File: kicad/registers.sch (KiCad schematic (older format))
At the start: 0 parts

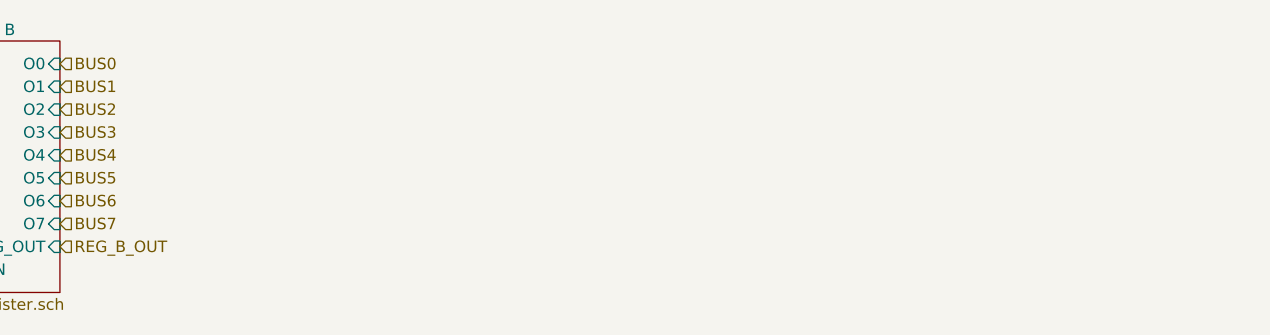
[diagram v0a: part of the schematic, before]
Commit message: Add M0-2 registers
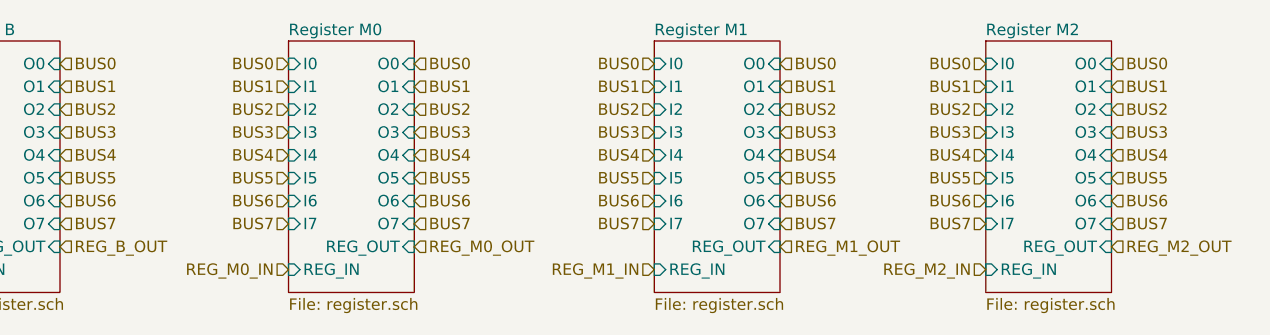
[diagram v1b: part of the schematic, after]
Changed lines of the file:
@@
 $Descr A4 11693 8268
 encoding utf-8
-Sheet 5 9
+Sheet 5 15
 Title ""
 Date ""
@@
 Text HLabel 3050 1650 2    50   Input ~ 0
 REG_B_OUT
+$Sheet
+S 4050 750  550  1100
+U 5AFCB536
+F0 "Register M0" 50
+F1 "register.sch" 50
+F2 "REG_IN" I L 4050 1750 50
+F3 "I0" I L 4050 850 50
+F4 "I1" I L 4050 950 50
+F5 "I2" I L 4050 1050 50
+F6 "I3" I L 4050 1150 50
+F7 "I4" I L 4050 1250 50
+F8 "I5" I L 4050 1350 50
+F9 "I6" I L 4050 1450 50
+F10 "I7" I L 4050 1550 50
+F11 "REG_OUT" I R 4600 1650 50
+F12 "O0" I R 4600 850 50
+F13 "O1" I R 4600 950 50
+F14 "O2" I R 4600 1050 50
+F15 "O3" I R 4600 1150 50
+F16 "O4" I R 4600 1250 50
+F17 "O5" I R 4600 1350 50
+F18 "O6" I R 4600 1450 50
+F19 "O7" I R 4600 1550 50
+$EndSheet
+Text HLabel 4050 850  0    50   Input ~ 0
+BUS0
+Text HLabel 4050 950  0    50   Input ~ 0
+BUS1
+Text HLabel 4050 1050 0    50   Input ~ 0
+BUS2
+Text HLabel 4050 1150 0    50   Input ~ 0
+BUS3
+Text HLabel 4050 1250 0    50   Input ~ 0
+BUS4
+Text HLabel 4050 1350 0    50   Input ~ 0
+BUS5
+Text HLabel 4050 1450 0    50   Input ~ 0
+BUS6
+Text HLabel 4050 1550 0    50   Input ~ 0
+BUS7
+Text HLabel 4600 850  2    50   Input ~ 0
+BUS0
+Text HLabel 4600 950  2    50   Input ~ 0
+BUS1
+Text HLabel 4600 1050 2    50   Input ~ 0
+BUS2
+Text HLabel 4600 1150 2    50   Input ~ 0
+BUS3
+Text HLabel 4600 1250 2    50   Input ~ 0
+BUS4
+Text HLabel 4600 1350 2    50   Input ~ 0
+BUS5
+Text HLabel 4600 1450 2    50   Input ~ 0
+BUS6
+Text HLabel 4600 1550 2    50   Input ~ 0
+BUS7
+Text HLabel 4050 1750 0    50   Input ~ 0
+REG_M0_IN
+Text HLabel 4600 1650 2    50   Input ~ 0
+REG_M0_OUT
+$Sheet
+S 5650 750  550  1100
+U 5AFCB55D
+F0 "Register M1" 50
+F1 "register.sch" 50
+F2 "REG_IN" I L 5650 1750 50
+F3 "I0" I L 5650 850 50
+F4 "I1" I L 5650 950 50
+F5 "I2" I L 5650 1050 50
+F6 "I3" I L 5650 1150 50
+F7 "I4" I L 5650 1250 50
+F8 "I5" I L 5650 1350 50
+F9 "I6" I L 5650 1450 50
+F10 "I7" I L 5650 1550 50
+F11 "REG_OUT" I R 6200 1650 50
+F12 "O0" I R 6200 850 50
+F13 "O1" I R 6200 950 50
+F14 "O2" I R 6200 1050 50
+F15 "O3" I R 6200 1150 50
+F16 "O4" I R 6200 1250 50
+F17 "O5" I R 6200 1350 50
+F18 "O6" I R 6200 1450 50
+F19 "O7" I R 6200 1550 50
+$EndSheet
+Text HLabel 5650 850  0    50   Input ~ 0
+BUS0
+Text HLabel 5650 950  0    50   Input ~ 0
+BUS1
+Text HLabel 5650 1050 0    50   Input ~ 0
+BUS2
+Text HLabel 5650 1150 0    50   Input ~ 0
+BUS3
+Text HLabel 5650 1250 0    50   Input ~ 0
+BUS4
+Text HLabel 5650 1350 0    50   Input ~ 0
+BUS5
+Text HLabel 5650 1450 0    50   Input ~ 0
+BUS6
+Text HLabel 5650 1550 0    50   Input ~ 0
+BUS7
+Text HLabel 6200 850  2    50   Input ~ 0
+BUS0
+Text HLabel 6200 950  2    50   Input ~ 0
+BUS1
+Text HLabel 6200 1050 2    50   Input ~ 0
+BUS2
+Text HLabel 6200 1150 2    50   Input ~ 0
+BUS3
+Text HLabel 6200 1250 2    50   Input ~ 0
+BUS4
+Text HLabel 6200 1350 2    50   Input ~ 0
+BUS5
+Text HLabel 6200 1450 2    50   Input ~ 0
+BUS6
+Text HLabel 6200 1550 2    50   Input ~ 0
+BUS7
+Text HLabel 5650 1750 0    50   Input ~ 0
+REG_M1_IN
+Text HLabel 6200 1650 2    50   Input ~ 0
+REG_M1_OUT
+$Sheet
+S 7100 750  550  1100
+U 5AFCB584
+F0 "Register M2" 50
+F1 "register.sch" 50
+F2 "REG_IN" I L 7100 1750 50
+F3 "I0" I L 7100 850 50
+F4 "I1" I L 7100 950 50
+F5 "I2" I L 7100 1050 50
+F6 "I3" I L 7100 1150 50
+F7 "I4" I L 7100 1250 50
+F8 "I5" I L 7100 1350 50
+F9 "I6" I L 7100 1450 50
+F10 "I7" I L 7100 1550 50
+F11 "REG_OUT" I R 7650 1650 50
+F12 "O0" I R 7650 850 50
+F13 "O1" I R 7650 950 50
+F14 "O2" I R 7650 1050 50
+F15 "O3" I R 7650 1150 50
+F16 "O4" I R 7650 1250 50
+F17 "O5" I R 7650 1350 50
+F18 "O6" I R 7650 1450 50
+F19 "O7" I R 7650 1550 50
+$EndSheet
+Text HLabel 7100 850  0    50   Input ~ 0
+BUS0
+Text HLabel 7100 950  0    50   Input ~ 0
+BUS1
+Text HLabel 7100 1050 0    50   Input ~ 0
+BUS2
+Text HLabel 7100 1150 0    50   Input ~ 0
+BUS3
+Text HLabel 7100 1250 0    50   Input ~ 0
+BUS4
+Text HLabel 7100 1350 0    50   Input ~ 0
+BUS5
+Text HLabel 7100 1450 0    50   Input ~ 0
+BUS6
+Text HLabel 7100 1550 0    50   Input ~ 0
+BUS7
+Text HLabel 7650 850  2    50   Input ~ 0
+BUS0
+Text HLabel 7650 950  2    50   Input ~ 0
+BUS1
+Text HLabel 7650 1050 2    50   Input ~ 0
+BUS2
+Text HLabel 7650 1150 2    50   Input ~ 0
+BUS3
+Text HLabel 7650 1250 2    50   Input ~ 0
+BUS4
+Text HLabel 7650 1350 2    50   Input ~ 0
+BUS5
+Text HLabel 7650 1450 2    50   Input ~ 0
+BUS6
+Text HLabel 7650 1550 2    50   Input ~ 0
+BUS7
+Text HLabel 7100 1750 0    50   Input ~ 0
+REG_M2_IN
+Text HLabel 7650 1650 2    50   Input ~ 0
+REG_M2_OUT
 $EndSCHEMATC

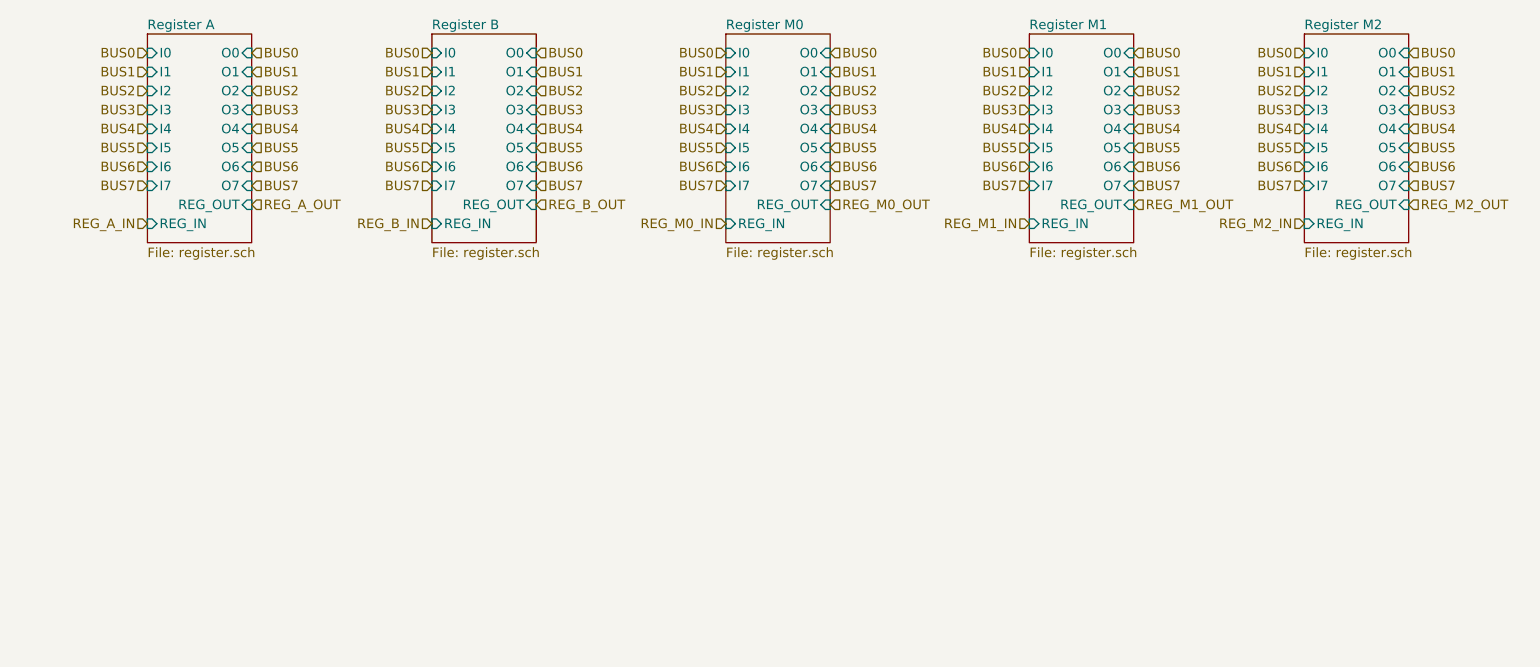
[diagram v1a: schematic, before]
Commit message: Remove register LEDs
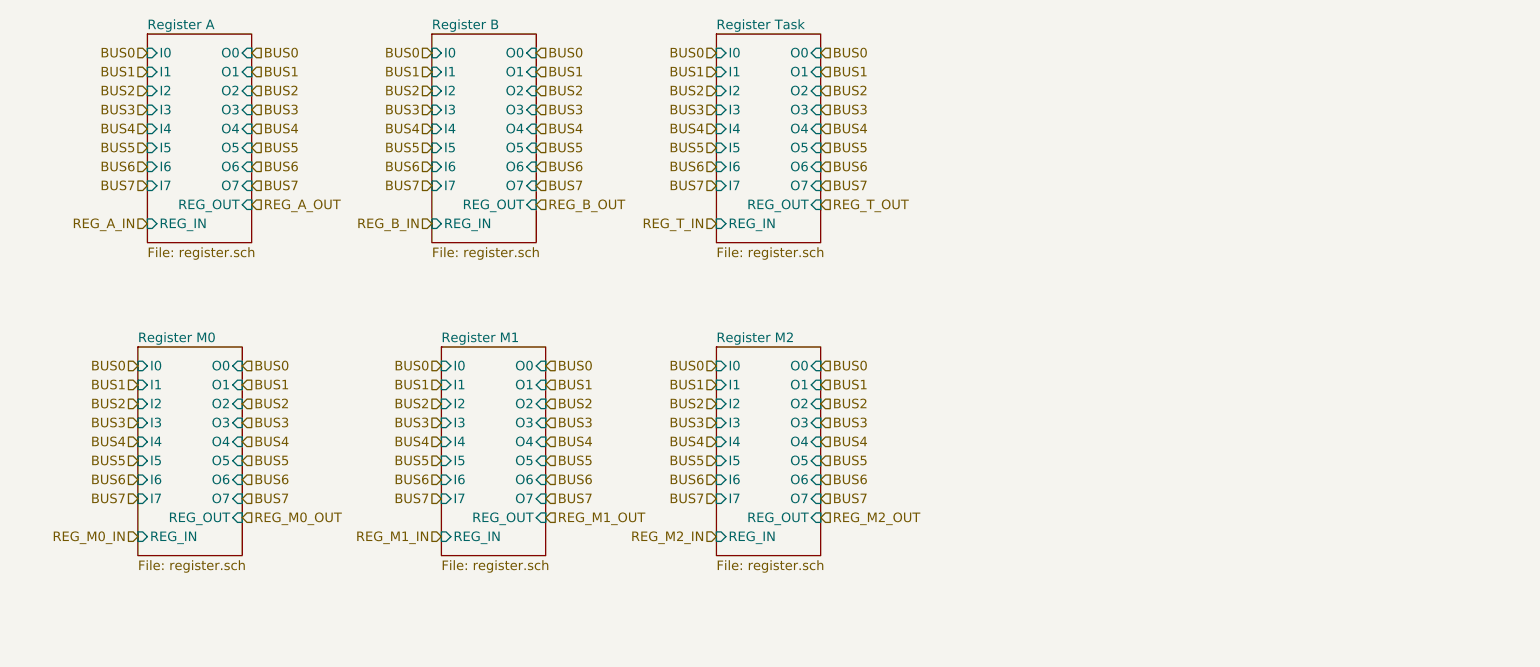
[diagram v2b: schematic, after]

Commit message: Add bus transceivers back just for registers A and B, so they can be connected to the ALU. Add ALU to schematic.
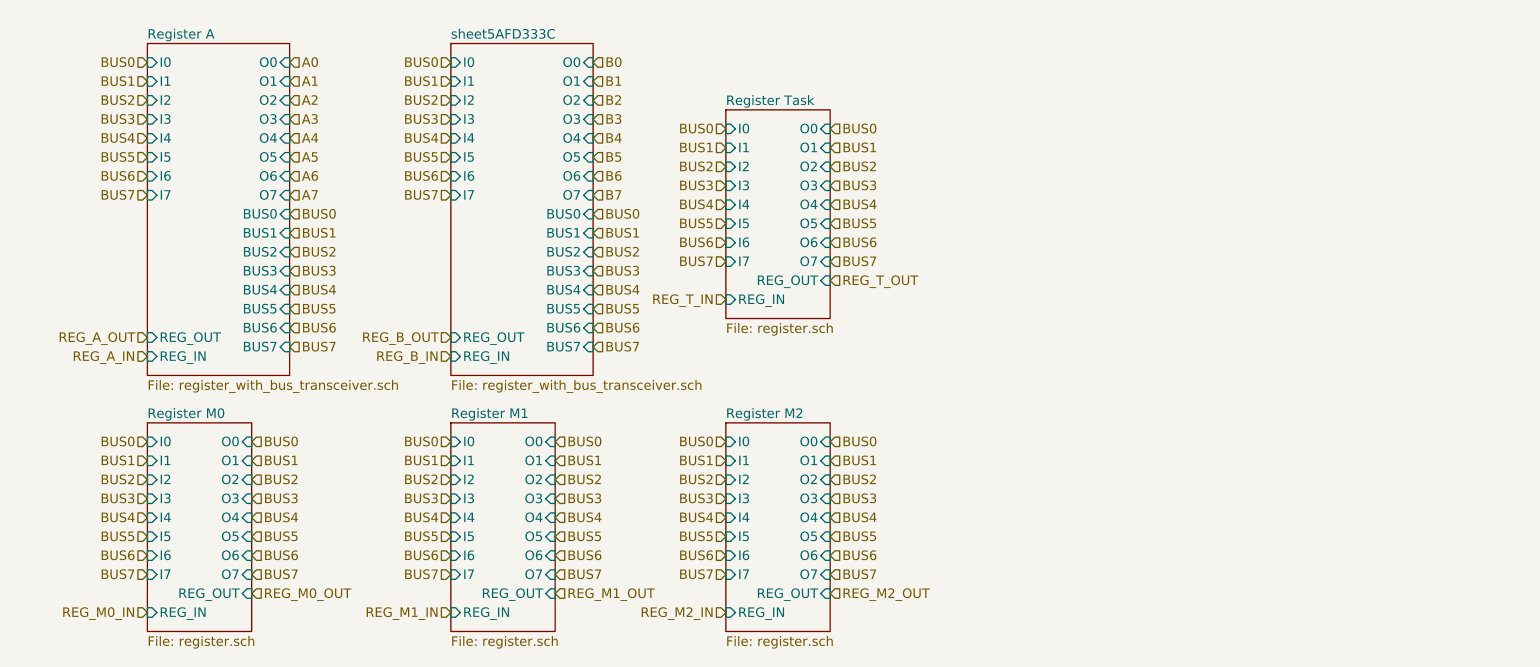
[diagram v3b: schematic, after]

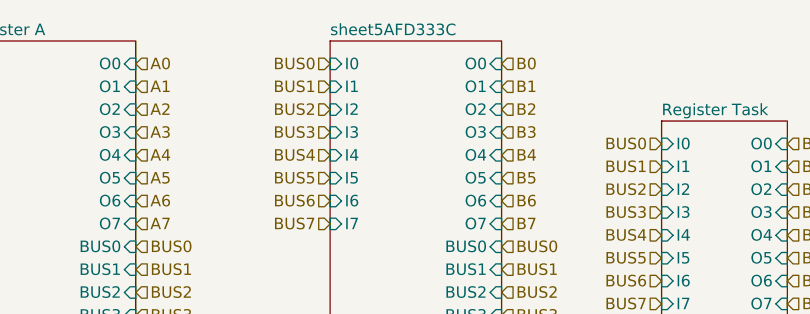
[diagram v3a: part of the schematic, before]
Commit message: Add display module. Still need to check if it needs resistors.
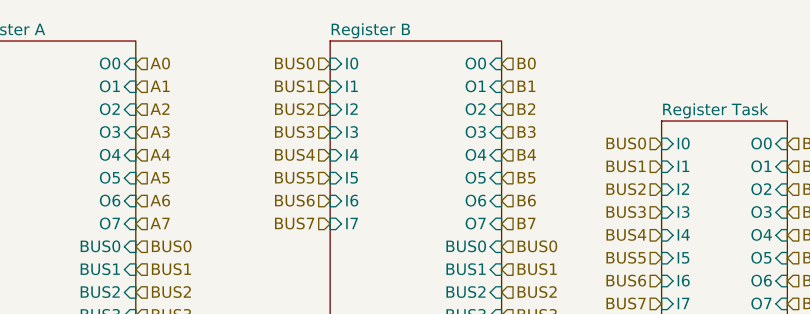
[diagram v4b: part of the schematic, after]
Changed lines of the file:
@@
 $Descr A4 11693 8268
 encoding utf-8
-Sheet 5 12
+Sheet 5 14
 Title ""
 Date ""
@@
 S 2600 800  750  1750
 U 5AFD336A
-F0 "sheet5AFD333C" 50
+F0 "Register B" 50
 F1 "register_with_bus_transceiver.sch" 50
 F2 "REG_IN" I L 2600 2450 50

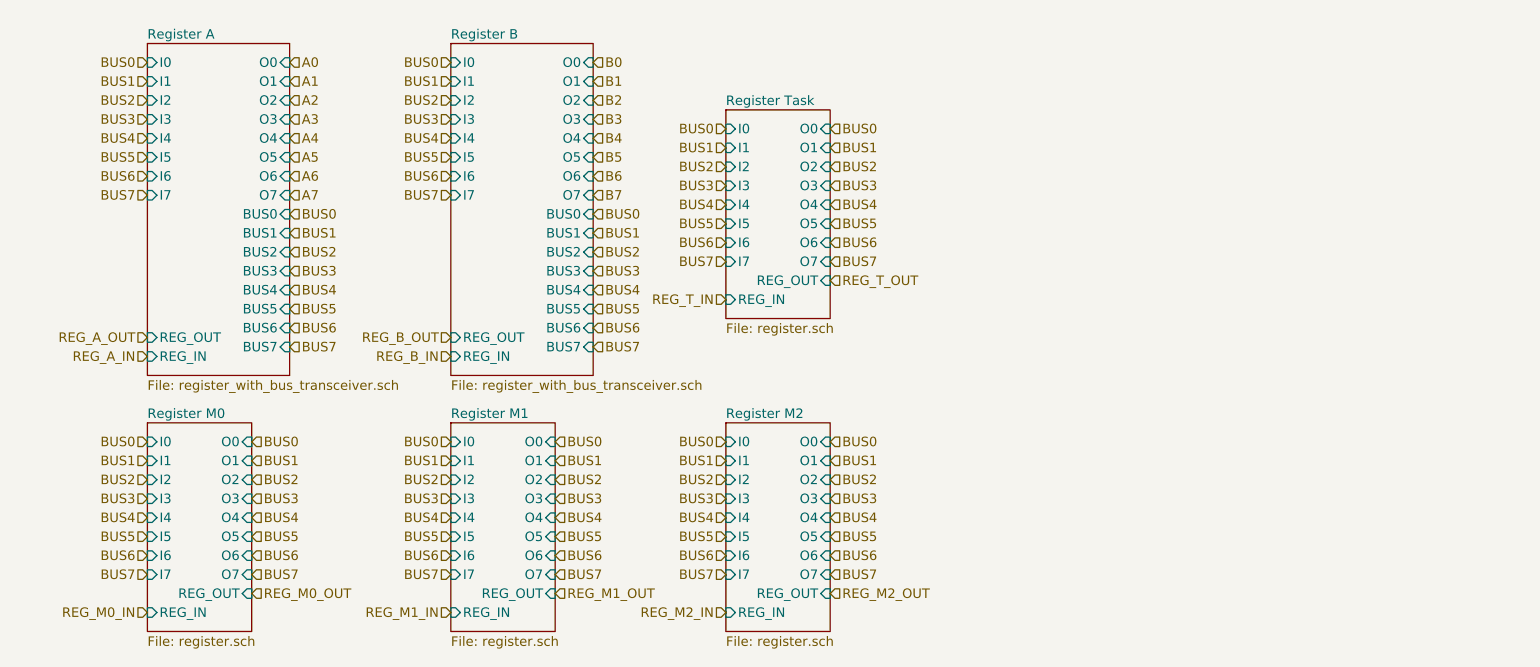
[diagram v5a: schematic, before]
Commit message: Schematic for kernel and user stack pointers.
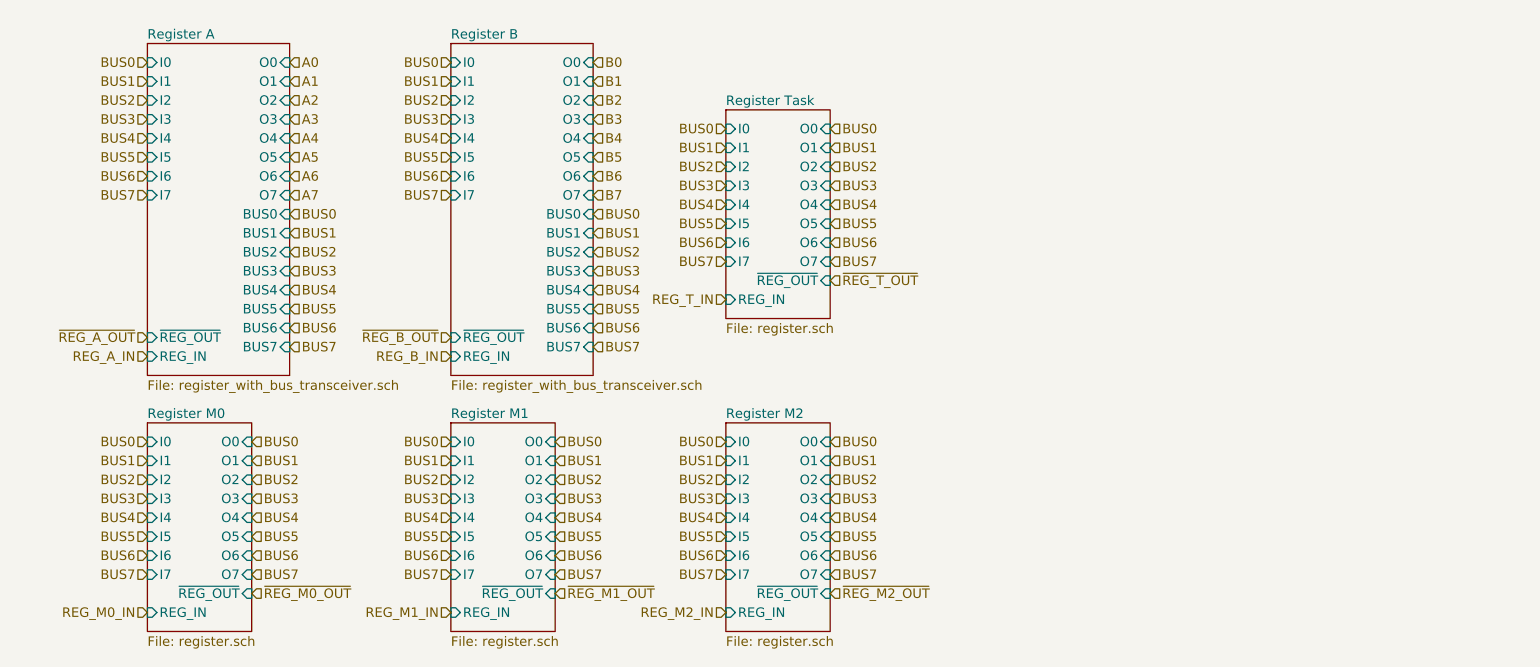
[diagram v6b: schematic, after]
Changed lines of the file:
@@
 $Descr A4 11693 8268
 encoding utf-8
-Sheet 5 17
+Sheet 5 19
 Title ""
 Date ""
@@
 REG_A_IN
 Text HLabel 1000 2350 0    50   Input ~ 0
-REG_A_OUT
+~REG_A_OUT
 Text HLabel 2600 2450 0    50   Input ~ 0
 REG_B_IN
 Text HLabel 2600 2350 0    50   Input ~ 0
-REG_B_OUT
+~REG_B_OUT
 $Sheet
 S 1000 2800 550  1100
@@
 F9 "I6" I L 1000 3500 50
 F10 "I7" I L 1000 3600 50
-F11 "REG_OUT" I R 1550 3700 50
+F11 "~REG_OUT" I R 1550 3700 50
 F12 "O0" I R 1550 2900 50
 F13 "O1" I R 1550 3000 50
@@
 REG_M0_IN
 Text HLabel 1550 3700 2    50   Input ~ 0
-REG_M0_OUT
+~REG_M0_OUT
 $Sheet
 S 2600 2800 550  1100
@@
 F9 "I6" I L 2600 3500 50
 F10 "I7" I L 2600 3600 50
-F11 "REG_OUT" I R 3150 3700 50
+F11 "~REG_OUT" I R 3150 3700 50
 F12 "O0" I R 3150 2900 50
 F13 "O1" I R 3150 3000 50
@@
 REG_M1_IN
 Text HLabel 3150 3700 2    50   Input ~ 0
-REG_M1_OUT
+~REG_M1_OUT
 $Sheet
 S 4050 2800 550  1100
@@
 F9 "I6" I L 4050 3500 50
 F10 "I7" I L 4050 3600 50
-F11 "REG_OUT" I R 4600 3700 50
+F11 "~REG_OUT" I R 4600 3700 50
 F12 "O0" I R 4600 2900 50
 F13 "O1" I R 4600 3000 50
@@
 REG_M2_IN
 Text HLabel 4600 3700 2    50   Input ~ 0
-REG_M2_OUT
+~REG_M2_OUT
 $Sheet
 S 4050 1150 550  1100
@@
 F9 "I6" I L 4050 1850 50
 F10 "I7" I L 4050 1950 50
-F11 "REG_OUT" I R 4600 2050 50
+F11 "~REG_OUT" I R 4600 2050 50
 F12 "O0" I R 4600 1250 50
 F13 "O1" I R 4600 1350 50
@@
 REG_T_IN
 Text HLabel 4600 2050 2    50   Input ~ 0
-REG_T_OUT
+~REG_T_OUT
 $Sheet
 S 1000 800  750  1750
@@
 F9 "I6" I L 1000 1500 50
 F10 "I7" I L 1000 1600 50
-F11 "REG_OUT" I L 1000 2350 50
+F11 "~REG_OUT" I L 1000 2350 50
 F12 "O0" I R 1750 900 50
 F13 "O1" I R 1750 1000 50
@@
 F9 "I6" I L 2600 1500 50
 F10 "I7" I L 2600 1600 50
-F11 "REG_OUT" I L 2600 2350 50
+F11 "~REG_OUT" I L 2600 2350 50
 F12 "O0" I R 3350 900 50
 F13 "O1" I R 3350 1000 50
